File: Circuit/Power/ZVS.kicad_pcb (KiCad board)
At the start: 2 copper layers, 81.3 x 55.9 mm, 16 parts, among them J1 12V DC in, J2 12V AC out, Q1 IRFP250, Q2 IRFP250, T1 5+5:10

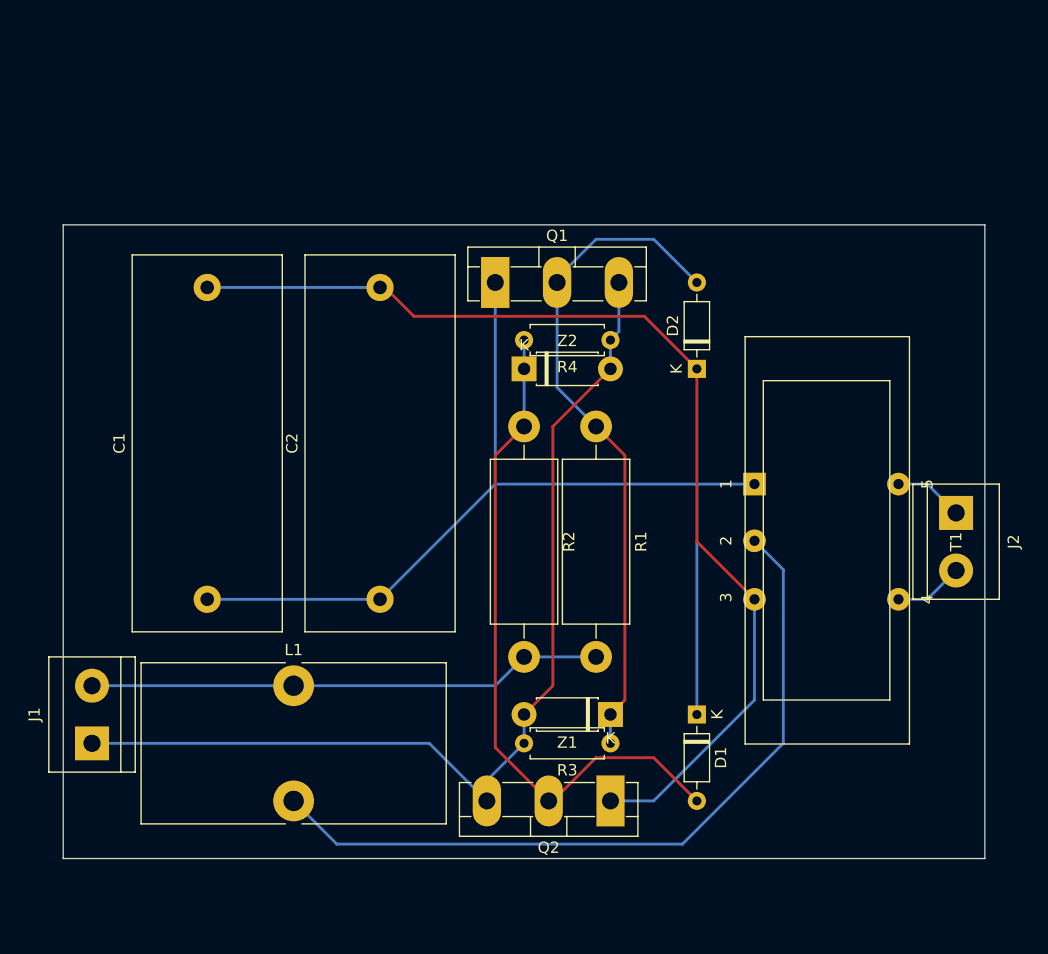
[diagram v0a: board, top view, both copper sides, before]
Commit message: [Circuit] Dual inductor variety of the ZVS module
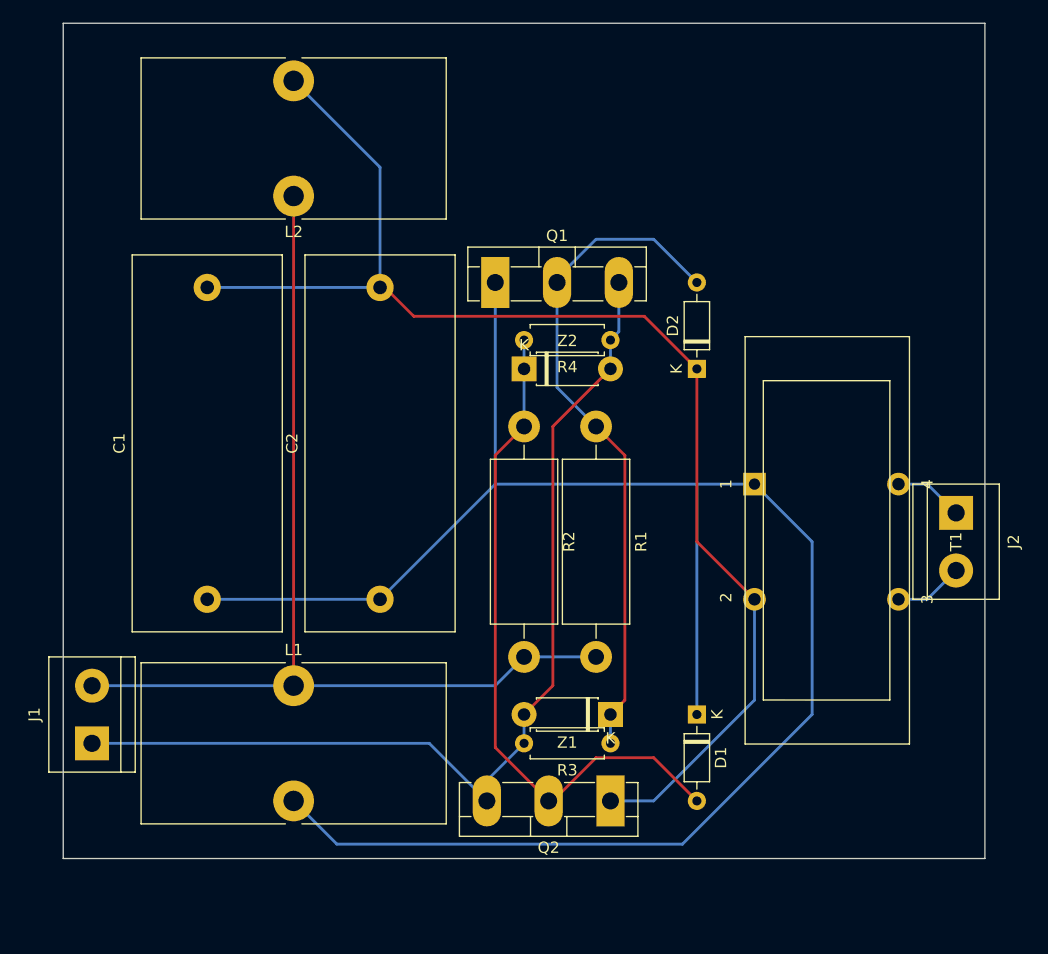
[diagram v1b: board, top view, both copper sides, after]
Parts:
- added L2: 100uH, Inductor_THT:L_Toroid_Vertical_L26.7mm_W14.0mm_P10.16mm_Pulse_D, F.Cu at (114.3, 22.9)
- R1, R2: value 2W/470 -> 470 2W
- T1: value 5+5:10 -> 10:10
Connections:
- L1 pad 2: Net-(L1-Pad2) -> Net-(C1-Pad1)
- T1 pad 2: Net-(L1-Pad2) -> Net-(C1-Pad2)
- T1 pad 3: Net-(C1-Pad2) -> /ACOutput-
- T1 pad 4: /ACOutput- -> /ACOutput+
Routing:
- net Net-(C1-Pad1): track 90.6 -> 165.0 mm
- net Net-(L1-Pad2): track 67.4 -> 0.00 mm
- net /DCInput+: track 45.5 -> 88.7 mm
- net Net-(C1-Pad2): track 93.9 -> 115.2 mm
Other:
- board size 81.3 x 55.9 mm -> 81.3 x 73.7 mm

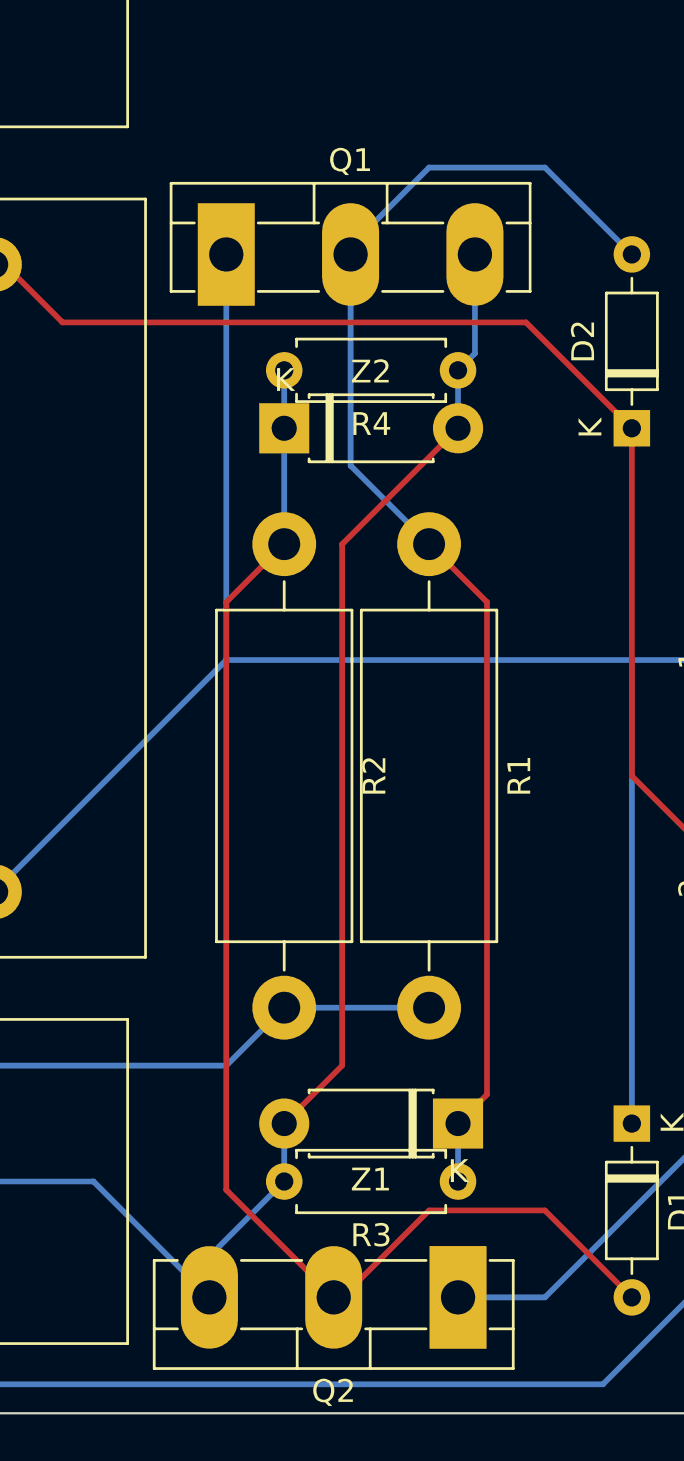
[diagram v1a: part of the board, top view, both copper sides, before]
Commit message: [Circuit] Rename the transformer in ZVS from 5pin to 4pin
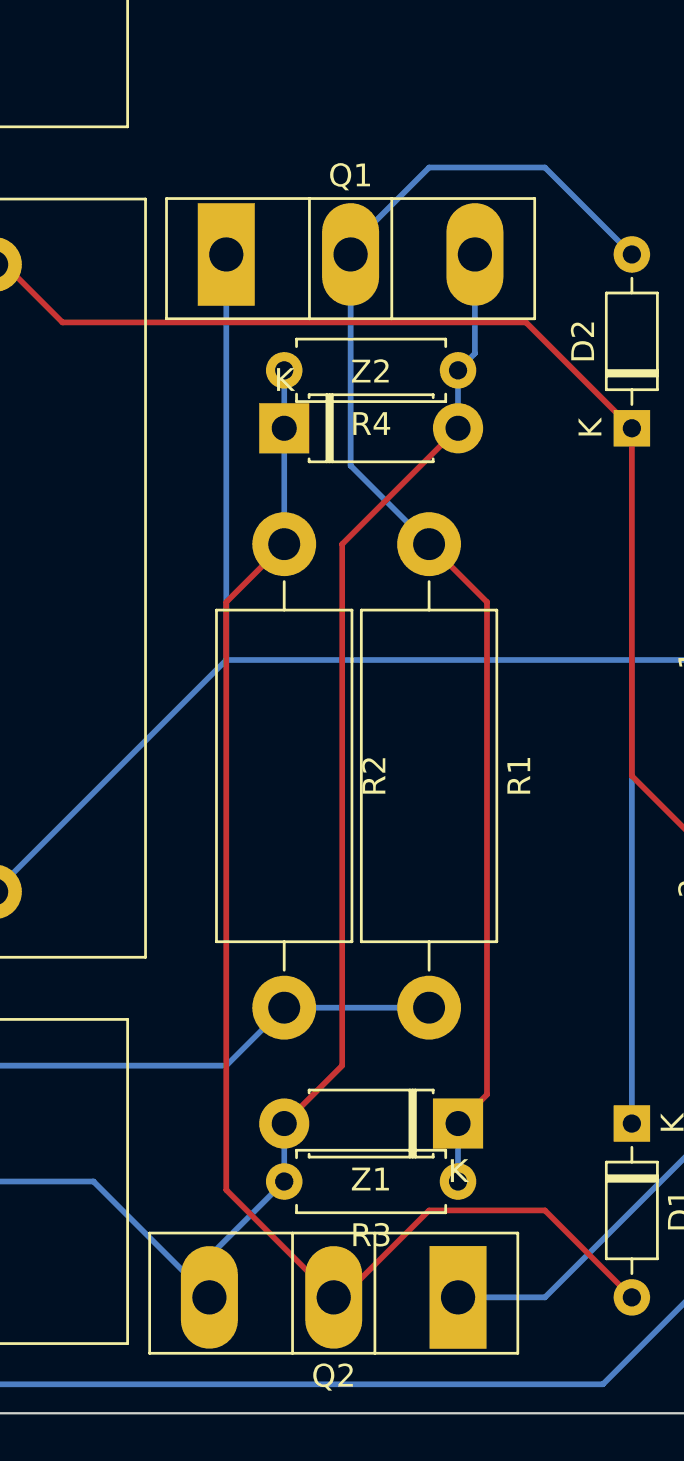
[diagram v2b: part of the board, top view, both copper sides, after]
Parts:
- Q1, Q2: footprint Package_TO_SOT_THT:TO-3P-3_Vertical -> Package_TO_SOT_THT:TO-247-3_Vertical
- T1: footprint Power:Transformer_Toroid_5Pin -> Power:Transformer_Toroid_4Pin
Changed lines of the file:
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@@
     (add_net "Net-(D2-Pad2)")
   )
-  (module Power:Transformer_Toroid_5Pin (layer F.Cu)
+  (module Power:Transformer_Toroid_4Pin (layer F.Cu)
     (at 154.94 40.64 270)
     (descr "Toroid Transformer")
@@
     )
   )
-  (module Package_TO_SOT_THT:TO-3P-3_Vertical (layer F.Cu)
+  (module Package_TO_SOT_THT:TO-247-3_Vertical (layer F.Cu)
     (at 142.24 76.2 180)
-    (descr "TO-3P-3, Vertical, RM 5.45mm, , see https://toshiba.semicon-storage.com/ap-en/design-support/package/detail.TO-3P(N).html")
-    (tags "TO-3P-3 Vertical RM 5.45mm ")
-    (fp_text reference Q2 (at 5.45 -4.12) (layer F.SilkS)
-      (effects (font (size 1 1) (thickness 0.15)))
-    )
-    (fp_text value IRFP250 (at 5.45 3.5) (layer F.Fab)
-      (effects (font (size 1 1) (thickness 0.15)))
-    )
-    (fp_text user %R (at 5.45 -4.12) (layer F.Fab)
-      (effects (font (size 1 1) (thickness 0.15)))
-    )
-    (fp_line (start 13.45 -3.25) (end -2.55 -3.25) (layer F.CrtYd) (width 0.05))
-    (fp_line (start 13.45 2.5) (end 13.45 -3.25) (layer F.CrtYd) (width 0.05))
-    (fp_line (start -2.55 2.5) (end 13.45 2.5) (layer F.CrtYd) (width 0.05))
-    (fp_line (start -2.55 -3.25) (end -2.55 2.5) (layer F.CrtYd) (width 0.05))
-    (fp_line (start 7.051 -3.12) (end 7.051 -1.38) (layer F.SilkS) (width 0.12))
-    (fp_line (start 3.85 -3.12) (end 3.85 -1.38) (layer F.SilkS) (width 0.12))
-    (fp_line (start 12.3 -1.38) (end 13.32 -1.38) (layer F.SilkS) (width 0.12))
-    (fp_line (start 6.85 -1.38) (end 9.5 -1.38) (layer F.SilkS) (width 0.12))
-    (fp_line (start 1.4 -1.38) (end 4.051 -1.38) (layer F.SilkS) (width 0.12))
-    (fp_line (start -2.42 -1.38) (end -1.4 -1.38) (layer F.SilkS) (width 0.12))
-    (fp_line (start 13.32 -3.12) (end 13.32 1.62) (layer F.SilkS) (width 0.12))
-    (fp_line (start -2.42 -3.12) (end -2.42 1.62) (layer F.SilkS) (width 0.12))
-    (fp_line (start 12.3 1.62) (end 13.32 1.62) (layer F.SilkS) (width 0.12))
-    (fp_line (start 6.85 1.62) (end 9.5 1.62) (layer F.SilkS) (width 0.12))
-    (fp_line (start 1.4 1.62) (end 4.051 1.62) (layer F.SilkS) (width 0.12))
-    (fp_line (start -2.42 1.62) (end -1.4 1.62) (layer F.SilkS) (width 0.12))
-    (fp_line (start -2.42 -3.12) (end 13.32 -3.12) (layer F.SilkS) (width 0.12))
-    (fp_line (start 7.05 -3) (end 7.05 -1.5) (layer F.Fab) (width 0.1))
-    (fp_line (start 3.85 -3) (end 3.85 -1.5) (layer F.Fab) (width 0.1))
-    (fp_line (start -2.3 -1.5) (end 13.2 -1.5) (layer F.Fab) (width 0.1))
-    (fp_line (start 13.2 -3) (end -2.3 -3) (layer F.Fab) (width 0.1))
-    (fp_line (start 13.2 1.5) (end 13.2 -3) (layer F.Fab) (width 0.1))
-    (fp_line (start -2.3 1.5) (end 13.2 1.5) (layer F.Fab) (width 0.1))
-    (fp_line (start -2.3 -3) (end -2.3 1.5) (layer F.Fab) (width 0.1))
+    (descr "TO-247-3, Vertical, RM 5.45mm, see https://toshiba.semicon-storage.com/us/product/mosfet/to-247-4l.html")
+    (tags "TO-247-3 Vertical RM 5.45mm")
+    (fp_text reference Q2 (at 5.45 -3.45) (layer F.SilkS)
+      (effects (font (size 1 1) (thickness 0.15)))
+    )
+    (fp_text value IRFP250 (at 5.45 3.95) (layer F.Fab)
+      (effects (font (size 1 1) (thickness 0.15)))
+    )
+    (fp_text user %R (at 5.45 -3.45) (layer F.Fab)
+      (effects (font (size 1 1) (thickness 0.15)))
+    )
+    (fp_line (start 13.65 -2.59) (end -2.75 -2.59) (layer F.CrtYd) (width 0.05))
+    (fp_line (start 13.65 2.95) (end 13.65 -2.59) (layer F.CrtYd) (width 0.05))
+    (fp_line (start -2.75 2.95) (end 13.65 2.95) (layer F.CrtYd) (width 0.05))
+    (fp_line (start -2.75 -2.59) (end -2.75 2.95) (layer F.CrtYd) (width 0.05))
+    (fp_line (start 7.255 -2.451) (end 7.255 2.82) (layer F.SilkS) (width 0.12))
+    (fp_line (start 3.646 -2.451) (end 3.646 2.82) (layer F.SilkS) (width 0.12))
+    (fp_line (start 13.52 -2.451) (end 13.52 2.82) (layer F.SilkS) (width 0.12))
+    (fp_line (start -2.62 -2.451) (end -2.62 2.82) (layer F.SilkS) (width 0.12))
+    (fp_line (start -2.62 2.82) (end 13.52 2.82) (layer F.SilkS) (width 0.12))
+    (fp_line (start -2.62 -2.451) (end 13.52 -2.451) (layer F.SilkS) (width 0.12))
+    (fp_line (start 7.255 -2.33) (end 7.255 2.7) (layer F.Fab) (width 0.1))
+    (fp_line (start 3.645 -2.33) (end 3.645 2.7) (layer F.Fab) (width 0.1))
+    (fp_line (start 13.4 -2.33) (end -2.5 -2.33) (layer F.Fab) (width 0.1))
+    (fp_line (start 13.4 2.7) (end 13.4 -2.33) (layer F.Fab) (width 0.1))
+    (fp_line (start -2.5 2.7) (end 13.4 2.7) (layer F.Fab) (width 0.1))
+    (fp_line (start -2.5 -2.33) (end -2.5 2.7) (layer F.Fab) (width 0.1))
     (pad 3 thru_hole oval (at 10.9 0 180) (size 2.5 4.5) (drill 1.5) (layers *.Cu *.Mask)
       (net 5 /DCInput-))
@@
     (pad 1 thru_hole rect (at 0 0 180) (size 2.5 4.5) (drill 1.5) (layers *.Cu *.Mask)
       (net 1 "Net-(C1-Pad2)"))
-    (model ${KISYS3DMOD}/Package_TO_SOT_THT.3dshapes/TO-3P-3_Vertical.wrl
-      (at (xyz 0 0 0))
-      (scale (xyz 1 1 1))
-      (rotate (xyz 0 0 0))
-    )
-  )
-  (module Package_TO_SOT_THT:TO-3P-3_Vertical (layer F.Cu)
+    (model ${KISYS3DMOD}/Package_TO_SOT_THT.3dshapes/TO-247-3_Vertical.wrl
+      (at (xyz 0 0 0))
+      (scale (xyz 1 1 1))
+      (rotate (xyz 0 0 0))
+    )
+  )
+  (module Package_TO_SOT_THT:TO-247-3_Vertical (layer F.Cu)
     (at 132.08 30.48)
-    (descr "TO-3P-3, Vertical, RM 5.45mm, , see https://toshiba.semicon-storage.com/ap-en/design-support/package/detail.TO-3P(N).html")
-    (tags "TO-3P-3 Vertical RM 5.45mm ")
-    (fp_text reference Q1 (at 5.45 -4.12) (layer F.SilkS)
-      (effects (font (size 1 1) (thickness 0.15)))
-    )
-    (fp_text value IRFP250 (at 5.45 3.5) (layer F.Fab)
-      (effects (font (size 1 1) (thickness 0.15)))
-    )
-    (fp_text user %R (at 5.45 -4.12) (layer F.Fab)
-      (effects (font (size 1 1) (thickness 0.15)))
-    )
-    (fp_line (start 13.45 -3.25) (end -2.55 -3.25) (layer F.CrtYd) (width 0.05))
-    (fp_line (start 13.45 2.5) (end 13.45 -3.25) (layer F.CrtYd) (width 0.05))
-    (fp_line (start -2.55 2.5) (end 13.45 2.5) (layer F.CrtYd) (width 0.05))
-    (fp_line (start -2.55 -3.25) (end -2.55 2.5) (layer F.CrtYd) (width 0.05))
-    (fp_line (start 7.051 -3.12) (end 7.051 -1.38) (layer F.SilkS) (width 0.12))
-    (fp_line (start 3.85 -3.12) (end 3.85 -1.38) (layer F.SilkS) (width 0.12))
-    (fp_line (start 12.3 -1.38) (end 13.32 -1.38) (layer F.SilkS) (width 0.12))
-    (fp_line (start 6.85 -1.38) (end 9.5 -1.38) (layer F.SilkS) (width 0.12))
-    (fp_line (start 1.4 -1.38) (end 4.051 -1.38) (layer F.SilkS) (width 0.12))
-    (fp_line (start -2.42 -1.38) (end -1.4 -1.38) (layer F.SilkS) (width 0.12))
-    (fp_line (start 13.32 -3.12) (end 13.32 1.62) (layer F.SilkS) (width 0.12))
-    (fp_line (start -2.42 -3.12) (end -2.42 1.62) (layer F.SilkS) (width 0.12))
-    (fp_line (start 12.3 1.62) (end 13.32 1.62) (layer F.SilkS) (width 0.12))
-    (fp_line (start 6.85 1.62) (end 9.5 1.62) (layer F.SilkS) (width 0.12))
-    (fp_line (start 1.4 1.62) (end 4.051 1.62) (layer F.SilkS) (width 0.12))
-    (fp_line (start -2.42 1.62) (end -1.4 1.62) (layer F.SilkS) (width 0.12))
-    (fp_line (start -2.42 -3.12) (end 13.32 -3.12) (layer F.SilkS) (width 0.12))
-    (fp_line (start 7.05 -3) (end 7.05 -1.5) (layer F.Fab) (width 0.1))
-    (fp_line (start 3.85 -3) (end 3.85 -1.5) (layer F.Fab) (width 0.1))
-    (fp_line (start -2.3 -1.5) (end 13.2 -1.5) (layer F.Fab) (width 0.1))
-    (fp_line (start 13.2 -3) (end -2.3 -3) (layer F.Fab) (width 0.1))
-    (fp_line (start 13.2 1.5) (end 13.2 -3) (layer F.Fab) (width 0.1))
-    (fp_line (start -2.3 1.5) (end 13.2 1.5) (layer F.Fab) (width 0.1))
-    (fp_line (start -2.3 -3) (end -2.3 1.5) (layer F.Fab) (width 0.1))
+    (descr "TO-247-3, Vertical, RM 5.45mm, see https://toshiba.semicon-storage.com/us/product/mosfet/to-247-4l.html")
+    (tags "TO-247-3 Vertical RM 5.45mm")
+    (fp_text reference Q1 (at 5.45 -3.45) (layer F.SilkS)
+      (effects (font (size 1 1) (thickness 0.15)))
+    )
+    (fp_text value IRFP250 (at 5.45 3.95) (layer F.Fab)
+      (effects (font (size 1 1) (thickness 0.15)))
+    )
+    (fp_text user %R (at 5.45 -3.45) (layer F.Fab)
+      (effects (font (size 1 1) (thickness 0.15)))
+    )
+    (fp_line (start 13.65 -2.59) (end -2.75 -2.59) (layer F.CrtYd) (width 0.05))
+    (fp_line (start 13.65 2.95) (end 13.65 -2.59) (layer F.CrtYd) (width 0.05))
+    (fp_line (start -2.75 2.95) (end 13.65 2.95) (layer F.CrtYd) (width 0.05))
+    (fp_line (start -2.75 -2.59) (end -2.75 2.95) (layer F.CrtYd) (width 0.05))
+    (fp_line (start 7.255 -2.451) (end 7.255 2.82) (layer F.SilkS) (width 0.12))
+    (fp_line (start 3.646 -2.451) (end 3.646 2.82) (layer F.SilkS) (width 0.12))
+    (fp_line (start 13.52 -2.451) (end 13.52 2.82) (layer F.SilkS) (width 0.12))
+    (fp_line (start -2.62 -2.451) (end -2.62 2.82) (layer F.SilkS) (width 0.12))
+    (fp_line (start -2.62 2.82) (end 13.52 2.82) (layer F.SilkS) (width 0.12))
+    (fp_line (start -2.62 -2.451) (end 13.52 -2.451) (layer F.SilkS) (width 0.12))
+    (fp_line (start 7.255 -2.33) (end 7.255 2.7) (layer F.Fab) (width 0.1))
+    (fp_line (start 3.645 -2.33) (end 3.645 2.7) (layer F.Fab) (width 0.1))
+    (fp_line (start 13.4 -2.33) (end -2.5 -2.33) (layer F.Fab) (width 0.1))
+    (fp_line (start 13.4 2.7) (end 13.4 -2.33) (layer F.Fab) (width 0.1))
+    (fp_line (start -2.5 2.7) (end 13.4 2.7) (layer F.Fab) (width 0.1))
+    (fp_line (start -2.5 -2.33) (end -2.5 2.7) (layer F.Fab) (width 0.1))
     (pad 3 thru_hole oval (at 10.9 0) (size 2.5 4.5) (drill 1.5) (layers *.Cu *.Mask)
       (net 5 /DCInput-))
@@
     (pad 1 thru_hole rect (at 0 0) (size 2.5 4.5) (drill 1.5) (layers *.Cu *.Mask)
       (net 2 "Net-(C1-Pad1)"))
-    (model ${KISYS3DMOD}/Package_TO_SOT_THT.3dshapes/TO-3P-3_Vertical.wrl
-      (at (xyz 0 0 0))
-      (scale (xyz 1 1 1))
+    (model ${KISYS3DMOD}/Package_TO_SOT_THT.3dshapes/TO-247-3_Vertical.wrl
+      (at (xyz 0 0 0))
+      (scale (xyz 1 1 1))
